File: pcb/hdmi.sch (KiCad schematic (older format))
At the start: 11 parts, among them U7 TPD12S016PWR, X7 HDMI_A

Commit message: yet another wip commit
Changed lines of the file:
@@
 encoding utf-8
 Sheet 12 12
-Title ""
+Title "WishMaster 1200"
 Date ""
-Rev ""
-Comp ""
-Comment1 ""
-Comment2 ""
+Rev "ES1"
+Comp "Konfusion"
+Comment1 "A1200 version (engineering prototype)"
+Comment2 "Wishmaster ARM \\ JIT turbo board for Amiga"
 Comment3 ""
 Comment4 ""
 $EndDescr
-Text GLabel 4100 4400 0    50   Input ~ 0
+Text GLabel 4100 4400 0    50   BiDi ~ 0
 FPGA_HDMI_D2+
-Text GLabel 4100 4300 0    50   Input ~ 0
+Text GLabel 4100 4300 0    50   BiDi ~ 0
 FPGA_HDMI_D2-
-Text GLabel 4100 4100 0    50   Input ~ 0
+Text GLabel 4100 4100 0    50   BiDi ~ 0
 FPGA_HDMI_D1+
-Text GLabel 4100 3800 0    50   Input ~ 0
+Text GLabel 4100 3800 0    50   BiDi ~ 0
 FPGA_HDMI_D0+
-Text GLabel 4100 3700 0    50   Input ~ 0
+Text GLabel 4100 3700 0    50   BiDi ~ 0
 FPGA_HDMI_D0-
-Text GLabel 4100 4000 0    50   Input ~ 0
+Text GLabel 4100 4000 0    50   BiDi ~ 0
 FPGA_HDMI_D1-
-Text GLabel 4100 3500 0    50   Input ~ 0
+Text GLabel 4100 3500 0    50   BiDi ~ 0
 FPGA_HDMI_CLK+
-Text GLabel 4100 3400 0    50   Input ~ 0
+Text GLabel 4100 3400 0    50   BiDi ~ 0
 FPGA_HDMI_CLK-
 $Comp

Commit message: pinout changes
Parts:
- renumbered R19 to R21, R20 to R22, R21 to R23, R22 to R24, R23 to R25
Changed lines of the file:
@@
 	6600 3350 6600 3450
 $Comp
-L Device:R R23
+L Device:R R25
 U 1 1 5E5DE66E
 P 7100 3700
-F 0 "R23" H 7170 3746 50  0000 L CNN
+F 0 "R25" H 7170 3746 50  0000 L CNN
 F 1 "1M" H 7170 3655 50  0000 L CNN
 F 2 "" V 7030 3700 50  0001 C CNN
@@
 FPGA_VCC3V3
 $Comp
-L Device:R R19
+L Device:R R21
 U 1 1 5E64A58C
 P 1850 2450
-F 0 "R19" V 1643 2450 50  0000 C CNN
+F 0 "R21" V 1643 2450 50  0000 C CNN
 F 1 "4.7k" V 1734 2450 50  0000 C CNN
 F 2 "" V 1780 2450 50  0001 C CNN
@@
 $EndComp
 $Comp
-L Device:R R20
+L Device:R R22
 U 1 1 5E64B262
 P 1850 2800
-F 0 "R20" V 2057 2800 50  0000 C CNN
+F 0 "R22" V 2057 2800 50  0000 C CNN
 F 1 "4.7k" V 1966 2800 50  0000 C CNN
 F 2 "" V 1780 2800 50  0001 C CNN
@@
 FPGA_VCC3V3
 $Comp
-L Device:R R21
+L Device:R R23
 U 1 1 5E655A52
 P 1850 3650
-F 0 "R21" V 1643 3650 50  0000 C CNN
+F 0 "R23" V 1643 3650 50  0000 C CNN
 F 1 "4.7k" V 1734 3650 50  0000 C CNN
 F 2 "" V 1780 3650 50  0001 C CNN
@@
 $EndComp
 $Comp
-L Device:R R22
+L Device:R R24
 U 1 1 5E655A58
 P 1850 4000
-F 0 "R22" V 2057 4000 50  0000 C CNN
+F 0 "R24" V 2057 4000 50  0000 C CNN
 F 1 "4.7k" V 1966 4000 50  0000 C CNN
 F 2 "" V 1780 4000 50  0001 C CNN

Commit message: testpoints footprints added, some footprints assigned
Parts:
- R21, R22, R23, R24, R25: footprint (none) -> Resistor_SMD:R_0603_1608Metric_Pad1.05x0.95mm_HandSolder
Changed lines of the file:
@@
 F 0 "R25" H 7170 3746 50  0000 L CNN
 F 1 "1M" H 7170 3655 50  0000 L CNN
-F 2 "" V 7030 3700 50  0001 C CNN
+F 2 "Resistor_SMD:R_0603_1608Metric_Pad1.05x0.95mm_HandSolder" V 7030 3700 50  0001 C CNN
 F 3 "~" H 7100 3700 50  0001 C CNN
 	1    7100 3700
@@
 F 0 "R21" V 1643 2450 50  0000 C CNN
 F 1 "4.7k" V 1734 2450 50  0000 C CNN
-F 2 "" V 1780 2450 50  0001 C CNN
+F 2 "Resistor_SMD:R_0603_1608Metric_Pad1.05x0.95mm_HandSolder" V 1780 2450 50  0001 C CNN
 F 3 "~" H 1850 2450 50  0001 C CNN
 	1    1850 2450
@@
 F 0 "R22" V 2057 2800 50  0000 C CNN
 F 1 "4.7k" V 1966 2800 50  0000 C CNN
-F 2 "" V 1780 2800 50  0001 C CNN
+F 2 "Resistor_SMD:R_0603_1608Metric_Pad1.05x0.95mm_HandSolder" V 1780 2800 50  0001 C CNN
 F 3 "~" H 1850 2800 50  0001 C CNN
 	1    1850 2800
@@
 F 0 "R23" V 1643 3650 50  0000 C CNN
 F 1 "4.7k" V 1734 3650 50  0000 C CNN
-F 2 "" V 1780 3650 50  0001 C CNN
+F 2 "Resistor_SMD:R_0603_1608Metric_Pad1.05x0.95mm_HandSolder" V 1780 3650 50  0001 C CNN
 F 3 "~" H 1850 3650 50  0001 C CNN
 	1    1850 3650
@@
 F 0 "R24" V 2057 4000 50  0000 C CNN
 F 1 "4.7k" V 1966 4000 50  0000 C CNN
-F 2 "" V 1780 4000 50  0001 C CNN
+F 2 "Resistor_SMD:R_0603_1608Metric_Pad1.05x0.95mm_HandSolder" V 1780 4000 50  0001 C CNN
 F 3 "~" H 1850 4000 50  0001 C CNN
 	1    1850 4000

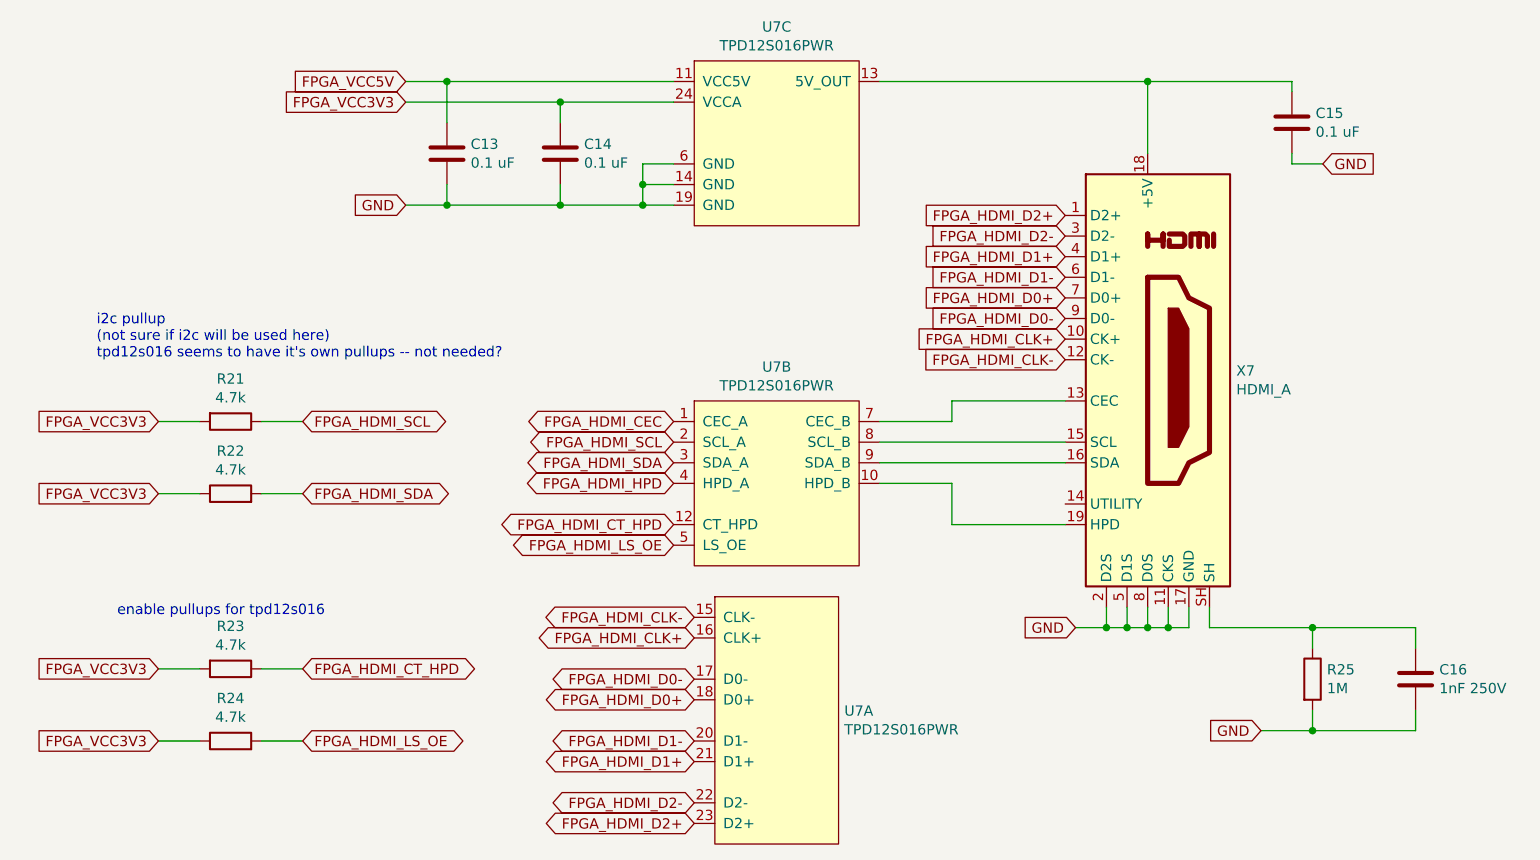
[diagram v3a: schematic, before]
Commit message: more footprints assigned
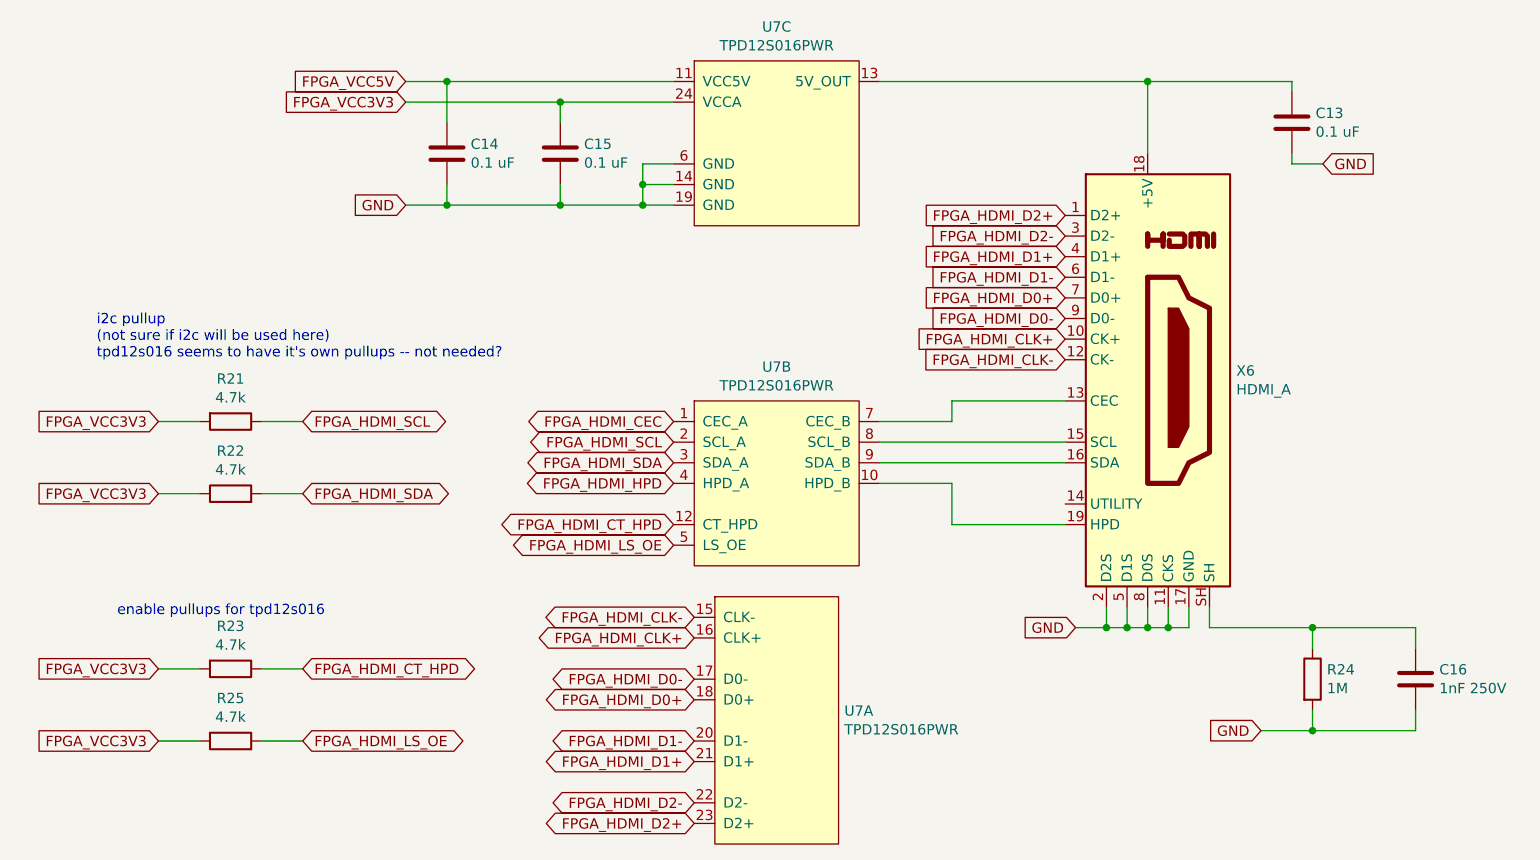
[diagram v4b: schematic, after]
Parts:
- U7: footprint (none) -> Package_SO:TSSOP-24_4.4x7.8mm_P0.65mm
- renumbered C15 to C13, C13 to C14, C14 to C15, R25 to R24, R24 to R25, X7 to X6
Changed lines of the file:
@@
 FPGA_HDMI_CLK-
 $Comp
-L Connector:HDMI_A X7
+L Connector:HDMI_A X6
 U 1 1 5E5A1311
 P 6300 2250
-F 0 "X7" H 6730 2296 50  0000 L CNN
+F 0 "X6" H 6730 2296 50  0000 L CNN
 F 1 "HDMI_A" H 6730 2205 50  0000 L CNN
 F 2 "" H 6325 2250 50  0001 C CNN
@@
 F 0 "U7" H 4828 5146 50  0000 L CNN
 F 1 "TPD12S016PWR" H 4828 5055 50  0000 L CNN
-F 2 "" H 4500 4250 50  0001 C CNN
+F 2 "Package_SO:TSSOP-24_4.4x7.8mm_P0.65mm" H 4500 4250 50  0001 C CNN
 F 3 "" H 4500 4250 50  0001 C CNN
 	1    4500 4500
@@
 F 0 "U7" H 4500 4115 50  0000 C CNN
 F 1 "TPD12S016PWR" H 4500 4024 50  0000 C CNN
-F 2 "" H 4500 2900 50  0001 C CNN
+F 2 "Package_SO:TSSOP-24_4.4x7.8mm_P0.65mm" H 4500 2900 50  0001 C CNN
 F 3 "" H 4500 2900 50  0001 C CNN
 	2    4500 3150
@@
 F 0 "U7" H 4500 2465 50  0000 C CNN
 F 1 "TPD12S016PWR" H 4500 2374 50  0000 C CNN
-F 2 "" H 4500 1250 50  0001 C CNN
+F 2 "Package_SO:TSSOP-24_4.4x7.8mm_P0.65mm" H 4500 1250 50  0001 C CNN
 F 3 "" H 4500 1250 50  0001 C CNN
 	3    4500 1500
@@
 	6600 3350 6600 3450
 $Comp
-L Device:R R25
+L Device:R R24
 U 1 1 5E5DE66E
 P 7100 3700
-F 0 "R25" H 7170 3746 50  0000 L CNN
+F 0 "R24" H 7170 3746 50  0000 L CNN
 F 1 "1M" H 7170 3655 50  0000 L CNN
 F 2 "Resistor_SMD:R_0603_1608Metric_Pad1.05x0.95mm_HandSolder" V 7030 3700 50  0001 C CNN
@@
 FPGA_VCC3V3
 $Comp
-L Device:C C14
+L Device:C C15
 U 1 1 5E5EFF65
 P 3450 1150
-F 0 "C14" H 3565 1196 50  0000 L CNN
+F 0 "C15" H 3565 1196 50  0000 L CNN
 F 1 "0.1 uF" H 3565 1105 50  0000 L CNN
 F 2 "" H 3488 1000 50  0001 C CNN
@@
 $EndComp
 $Comp
-L Device:C C13
+L Device:C C14
 U 1 1 5E5F9337
 P 2900 1150
-F 0 "C13" H 3015 1196 50  0000 L CNN
+F 0 "C14" H 3015 1196 50  0000 L CNN
 F 1 "0.1 uF" H 3015 1105 50  0000 L CNN
 F 2 "" H 2938 1000 50  0001 C CNN
@@
 Connection ~ 3850 1400
 $Comp
-L Device:C C15
+L Device:C C13
 U 1 1 5E6181E4
 P 7000 1000
-F 0 "C15" H 7115 1046 50  0000 L CNN
+F 0 "C13" H 7115 1046 50  0000 L CNN
 F 1 "0.1 uF" H 7115 955 50  0000 L CNN
 F 2 "" H 7038 850 50  0001 C CNN
@@
 $EndComp
 $Comp
-L Device:R R24
+L Device:R R25
 U 1 1 5E655A58
 P 1850 4000
-F 0 "R24" V 2057 4000 50  0000 C CNN
+F 0 "R25" V 2057 4000 50  0000 C CNN
 F 1 "4.7k" V 1966 4000 50  0000 C CNN
 F 2 "Resistor_SMD:R_0603_1608Metric_Pad1.05x0.95mm_HandSolder" V 1780 4000 50  0001 C CNN

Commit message: more footprints assigned, caps added into open collector base circuit
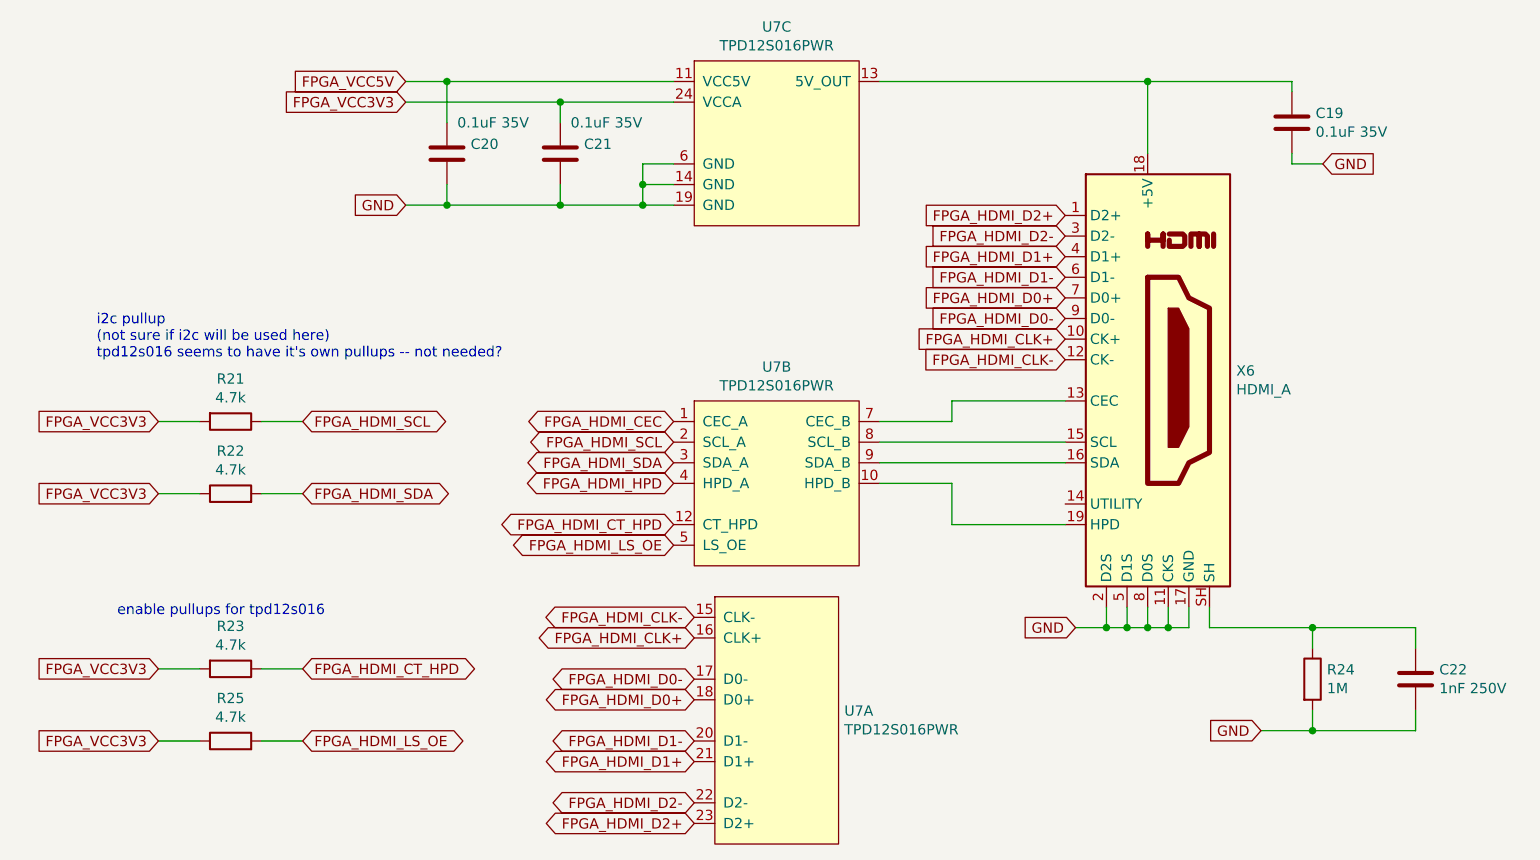
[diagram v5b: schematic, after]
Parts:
- C19: renamed from C13; value 0.1 uF -> 0.1uF 35V; footprint (none) -> Capacitor_SMD:C_0603_1608Metric_Pad1.05x0.95mm_HandSolder
- C20: renamed from C14; value 0.1 uF -> 0.1uF 35V; footprint (none) -> Capacitor_SMD:C_0603_1608Metric_Pad1.05x0.95mm_HandSolder
- C21: renamed from C15; value 0.1 uF -> 0.1uF 35V; footprint (none) -> Capacitor_SMD:C_0603_1608Metric_Pad1.05x0.95mm_HandSolder
- C22: renamed from C16; footprint (none) -> Capacitor_SMD:C_0603_1608Metric_Pad1.05x0.95mm_HandSolder
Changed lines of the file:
@@
 $EndComp
 $Comp
-L Device:C C16
+L Device:C C22
 U 1 1 5E5DF93C
 P 7600 3700
-F 0 "C16" H 7715 3746 50  0000 L CNN
+F 0 "C22" H 7715 3746 50  0000 L CNN
 F 1 "1nF 250V" H 7715 3655 50  0000 L CNN
-F 2 "" H 7638 3550 50  0001 C CNN
+F 2 "Capacitor_SMD:C_0603_1608Metric_Pad1.05x0.95mm_HandSolder" H 7638 3550 50  0001 C CNN
 F 3 "~" H 7600 3700 50  0001 C CNN
 	1    7600 3700
@@
 FPGA_VCC3V3
 $Comp
-L Device:C C15
+L Device:C C21
 U 1 1 5E5EFF65
 P 3450 1150
-F 0 "C15" H 3565 1196 50  0000 L CNN
-F 1 "0.1 uF" H 3565 1105 50  0000 L CNN
-F 2 "" H 3488 1000 50  0001 C CNN
+F 0 "C21" H 3565 1196 50  0000 L CNN
+F 1 "0.1uF 35V" H 3500 1300 50  0000 L CNN
+F 2 "Capacitor_SMD:C_0603_1608Metric_Pad1.05x0.95mm_HandSolder" H 3488 1000 50  0001 C CNN
 F 3 "~" H 3450 1150 50  0001 C CNN
 	1    3450 1150
@@
 $EndComp
 $Comp
-L Device:C C14
+L Device:C C20
 U 1 1 5E5F9337
 P 2900 1150
-F 0 "C14" H 3015 1196 50  0000 L CNN
-F 1 "0.1 uF" H 3015 1105 50  0000 L CNN
-F 2 "" H 2938 1000 50  0001 C CNN
+F 0 "C20" H 3015 1196 50  0000 L CNN
+F 1 "0.1uF 35V" H 2950 1300 50  0000 L CNN
+F 2 "Capacitor_SMD:C_0603_1608Metric_Pad1.05x0.95mm_HandSolder" H 2938 1000 50  0001 C CNN
 F 3 "~" H 2900 1150 50  0001 C CNN
 	1    2900 1150
@@
 Connection ~ 3850 1400
 $Comp
-L Device:C C13
+L Device:C C19
 U 1 1 5E6181E4
 P 7000 1000
-F 0 "C13" H 7115 1046 50  0000 L CNN
-F 1 "0.1 uF" H 7115 955 50  0000 L CNN
-F 2 "" H 7038 850 50  0001 C CNN
+F 0 "C19" H 7115 1046 50  0000 L CNN
+F 1 "0.1uF 35V" H 7115 955 50  0000 L CNN
+F 2 "Capacitor_SMD:C_0603_1608Metric_Pad1.05x0.95mm_HandSolder" H 7038 850 50  0001 C CNN
 F 3 "~" H 7000 1000 50  0001 C CNN
 	1    7000 1000

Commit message: working on pcb
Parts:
- X6: footprint (none) -> WM1200:HDMI-19-02F
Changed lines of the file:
@@
 F 0 "X6" H 6730 2296 50  0000 L CNN
 F 1 "HDMI_A" H 6730 2205 50  0000 L CNN
-F 2 "" H 6325 2250 50  0001 C CNN
+F 2 "WM1200:HDMI-19-02F" H 6325 2250 50  0001 C CNN
 F 3 "https://en.wikipedia.org/wiki/HDMI" H 6325 2250 50  0001 C CNN
 	1    6300 2250
